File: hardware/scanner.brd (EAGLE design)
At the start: 65 x 56 mm, 9 parts, among them K1 PIN20X2, U1 EEPROM24, U2 TPS61165DBV

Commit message: update hat
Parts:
- removed CFG: (no value), FLYFISH:PIN_W_2
- added JP1, POWER: (no value), pinhead:1X02
- SWITCH: device FLYFISH:PIN_W_2 -> pinhead:1X02
- U1: value EEPROM24 -> CAT24C32WI-GT3; device FLYFISH:SOIC8 -> mbed-HDK-IC:SOIC127P600X175-8N
- moved SWITCH 51.6 mm to (28.0, 41.0), turned to 0 degrees
- moved U2 51.4 mm to (9.00, 44.0), turned to 180 degrees
- moved C1 8.25 mm to (56.0, 39.0), turned to 90 degrees
- moved R3 6.80 mm to (58.0, 39.0), turned to 90 degrees
- moved U1 6.76 mm to (59.0, 44.0), turned to 0 degrees
- moved R2 5.67 mm to (60.0, 39.0), turned to 270 degrees
- moved R1 3.16 mm to (62.0, 39.0), turned to 270 degrees
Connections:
- new net N$6: JP1.1, R3.2, U1.7
- net +3V3: now also R3.1; no longer R3.2
- net GND: now also JP1.2, POWER.1, SWITCH.1; no longer CFG.2, SWITCH.2
- net N$1: now also U1.5; no longer U1.6
- net N$2: now also POWER.2; no longer K1.27, R2.1, U1.5
- net N$3: now also K1.27, R2.1, U1.6; no longer CFG.1, R3.1, U1.7
- net N$4: now also SWITCH.2; no longer SWITCH.1
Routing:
- net +3V3: track 0.00 -> 57.2 mm
- net GND: track 0.00 -> 50.4 mm, vias 0 -> 2
- net N$1: track 0.00 -> 32.0 mm, vias 0 -> 1
- net N$3: track 0.00 -> 29.8 mm, vias 0 -> 1
- net N$5: track 0.00 -> 18.9 mm, vias 0 -> 1
- net N$6: track 0.00 -> 18.8 mm, vias 0 -> 1
- net +5V: track 0.00 -> 16.1 mm

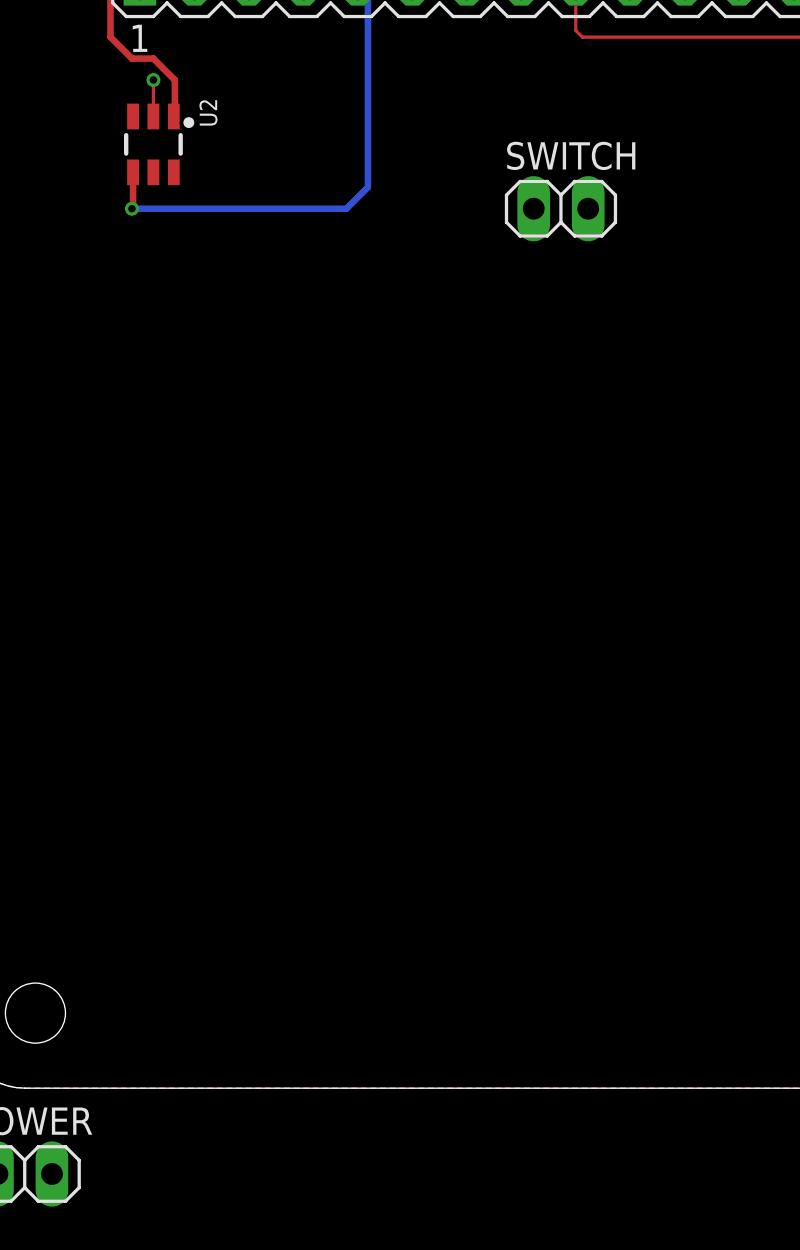
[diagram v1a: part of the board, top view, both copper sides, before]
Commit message: move eagle libs
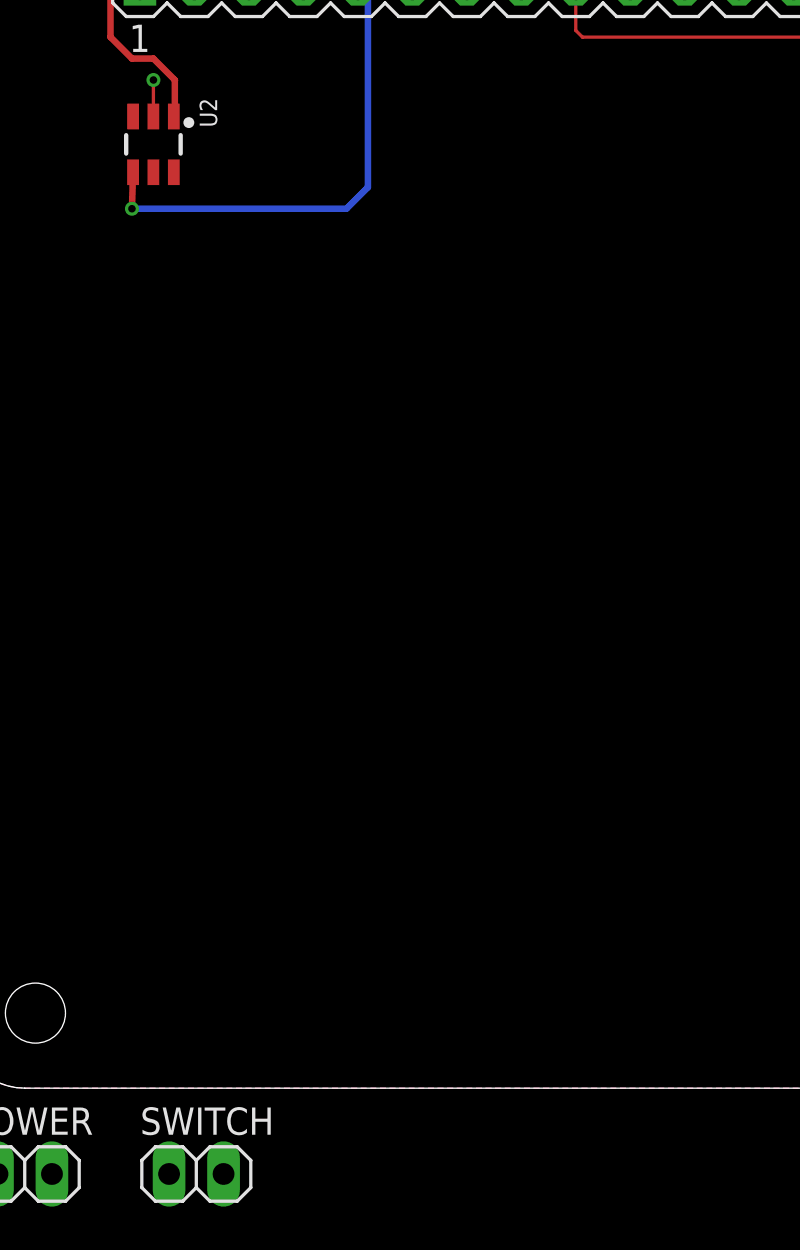
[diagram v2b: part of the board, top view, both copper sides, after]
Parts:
- moved SWITCH 48.1 mm to (11.0, -4.00)
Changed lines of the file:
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@@
 <drawing>
 <settings>
-<setting alwaysvectorfont="yes"/>
+<setting alwaysvectorfont="no"/>
 <setting keepoldvectorfont="yes"/>
 <setting verticaltext="up"/>
@@
 <attribute name="VALUE" x="60.286" y="37.984" size="1.27" layer="27" rot="R90"/>
 </element>
-<element name="SWITCH" library="pinhead" library_urn="urn:adsk.eagle:library:325" package="1X02" package3d_urn="urn:adsk.eagle:package:22435/2" value="" x="28" y="41" smashed="yes">
-<attribute name="NAME" x="25.3838" y="42.8288" size="1.27" layer="25" ratio="10"/>
-<attribute name="VALUE" x="25.46" y="37.825" size="1.27" layer="27"/>
+<element name="SWITCH" library="pinhead" library_urn="urn:adsk.eagle:library:325" package="1X02" package3d_urn="urn:adsk.eagle:package:22435/2" value="" x="11" y="-4" smashed="yes">
+<attribute name="NAME" x="8.3838" y="-2.1712" size="1.27" layer="25" ratio="10"/>
+<attribute name="VALUE" x="8.46" y="-7.175" size="1.27" layer="27"/>
 </element>
 <element name="JP1" library="pinhead" library_urn="urn:adsk.eagle:library:325" package="1X02" package3d_urn="urn:adsk.eagle:package:22435/2" value="" x="59" y="34" smashed="yes">
@@
 <wire x1="58" y1="36" x2="57" y2="37" width="0.1524" layer="16"/>
 <wire x1="57" y1="37" x2="57" y2="48" width="0.1524" layer="16"/>
-<via x="8" y="41" extent="1-16" drill="0.35"/>
-<wire x1="8.05" y1="41.05" x2="8" y2="41" width="0.1524" layer="1"/>
 <wire x1="19" y1="42" x2="18" y2="41" width="0.3048" layer="16"/>
-<wire x1="18" y1="41" x2="8" y2="41" width="0.3048" layer="16"/>
 <wire x1="18.53" y1="51.23" x2="19" y2="50.76" width="0.3048" layer="16"/>
 <wire x1="19" y1="50.76" x2="19" y2="42" width="0.3048" layer="16"/>
-<wire x1="8.05" y1="42.6999" x2="8.05" y2="41.05" width="0.3048" layer="1"/>
 <contactref element="POWER" pad="1"/>
+<wire x1="18" y1="41" x2="8" y2="41" width="0.3048" layer="16"/>
+<via x="8" y="41" extent="1-16" drill="0.35"/>
+<wire x1="8" y1="41" x2="8.05" y2="42.6999" width="0.3048" layer="1"/>
 <wire x1="43.93" y1="53.77" x2="49.01" y2="53.77" width="0" layer="19" extent="1-1"/>
 <wire x1="38.85" y1="51.23" x2="43.93" y2="53.77" width="0" layer="19" extent="1-1"/>
@@
 <wire x1="19" y1="50.76" x2="23.61" y2="53.77" width="0" layer="19" extent="16-16"/>
 <wire x1="13.45" y1="53.77" x2="18.53" y2="51.23" width="0" layer="19" extent="1-1"/>
-<wire x1="26.73" y1="41" x2="19" y2="42" width="0" layer="19" extent="16-16"/>
+<wire x1="9.73" y1="-4" x2="19" y2="42" width="0" layer="19" extent="16-16"/>
 <wire x1="1.73" y1="-4" x2="8" y2="41" width="0" layer="19" extent="16-16"/>
 </signal>
@@
 <contactref element="K1" pad="16"/>
 <contactref element="SWITCH" pad="2"/>
-<wire x1="29.27" y1="41" x2="26.15" y2="53.77" width="0" layer="19" extent="1-1"/>
+<wire x1="12.27" y1="-4" x2="26.15" y2="53.77" width="0" layer="19" extent="1-1"/>
 </signal>
 <signal name="N$5">

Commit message: update pcb
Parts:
- added C2: 220nF, resistor:C0805K
- added C3: 4.7μF, resistor:C0805K
- added C4: 1μF, resistor:C0805K
- added D1: 40V 550mA, adafruit:SOD-123
- added L1: 10 μH ±20% 1.49A, m-pad-2.1:D53LC
- added LED1, LED2: LW_W5SM-JYKY-JKQL-1, LW_W5SM-JYKY-JKQL-1:LWW5SMJYKYJKQL1
- added LED3, LED4, LED5: (no value), led:CHIP-LED0805
- added R4: 0.57, resistor:M0805
- added R5, R6, R7: 330, resistor:M0805
- moved POWER 30.6 mm to (33.0, -10.0)
- moved SWITCH 22.1 mm to (33.0, -6.00)
- moved C1 7.81 mm to (62.0, 34.0), turned to 270 degrees
- moved U2 5.83 mm to (6.00, 39.0)
- moved JP1 1.00 mm to (58.0, 34.0)
- moved R1 1.00 mm to (61.0, 39.0)
- moved R2 1.00 mm to (59.0, 39.0)
- moved R3 1.00 mm to (57.0, 39.0)
- moved U1 1.00 mm to (59.0, 45.0)
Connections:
- new net N$10: C4.1, D1.C, LED1.2
- new net N$11: LED1.1, LED2.2
- new net N$13: LED3.A, R5.2
- new net N$16: K1.13, R6.1
- new net N$17: LED4.A, R6.2
- new net N$18: LED5.A, R7.2
- new net N$19: K1.11, R5.1
- new net N$20: K1.15, R7.1
- new net N$7: C2.1, U2.5
- new net N$8: LED2.1, R4.1, U2.6
- new net N$9: D1.A, L1.2, U2.3
- net +5V: now also C3.1, L1.1
- net GND: now also C2.2, C3.2, C4.2, LED3.C, LED4.C, LED5.C, R4.2
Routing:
- net N$8: track 0.00 -> 79.7 mm
- net N$11: track 0.00 -> 55.4 mm
- net N$20: track 0.00 -> 52.1 mm, vias 0 -> 1
- net N$16: track 0.00 -> 50.6 mm, vias 0 -> 1
- net N$19: track 0.00 -> 50.2 mm, vias 0 -> 1
- net GND: track 50.4 -> 18.2 mm, vias 2 -> 6
- net N$10: track 0.00 -> 22.6 mm
- net N$9: track 0.00 -> 10.9 mm
- net N$5: track 18.9 -> 26.9 mm
- net +5V: track 16.1 -> 20.6 mm
- net +3V3: track 57.2 -> 61.5 mm
- net N$18: track 0.00 -> 2.00 mm
- net N$17: track 0.00 -> 2.00 mm
- net N$13: track 0.00 -> 2.00 mm
- net N$7: track 0.00 -> 1.70 mm
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- added copper zone on layer 2, net GND
- removed copper zone on layer 1, net GND
- removed copper zone on layer 16, net GND

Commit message: update pcb
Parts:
- removed POWER: (no value), pinhead:1X02
- added JP2: (no value), pinhead:2X02
- moved SWITCH 33.1 mm to (4.00, 10.0), turned to 180 degrees
- moved JP1 11.2 mm to (53.0, 44.0), turned to 90 degrees
- moved C1 3.61 mm to (59.0, 36.0), turned to 180 degrees
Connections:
- removed net N$2: POWER.2
- net +5V: now also JP2.1, JP2.2
- net GND: now also JP2.3, JP2.4; no longer POWER.1
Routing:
- net N$4: track 0.00 -> 63.6 mm
- net +5V: track 20.6 -> 61.9 mm
- net GND: track 18.2 -> 24.2 mm, vias 6 -> 8
- net N$6: track 17.2 -> 12.9 mm
- net +3V3: track 61.5 -> 63.1 mm
- net N$19: track 50.2 -> 51.4 mm
- net N$16: track 50.6 -> 51.8 mm
- net N$20: track 52.1 -> 53.3 mm

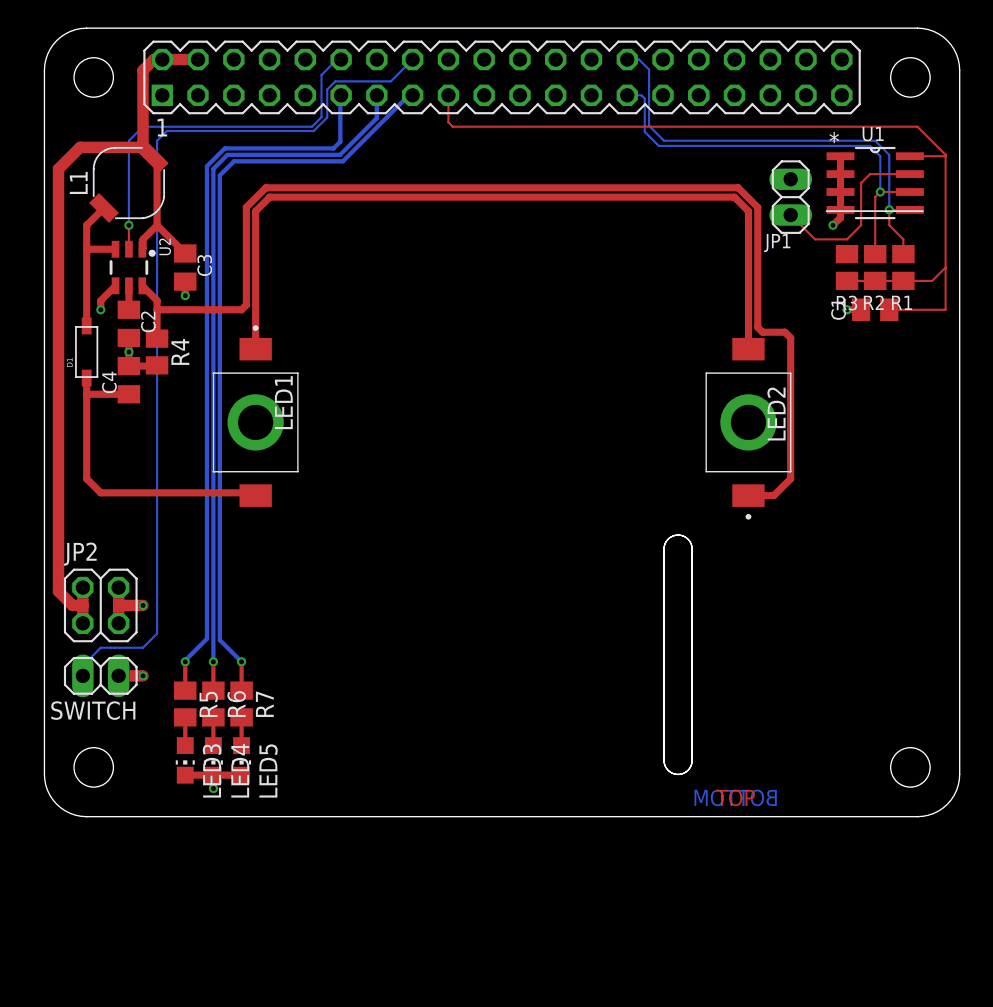
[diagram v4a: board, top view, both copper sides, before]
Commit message: added camera mounting holes
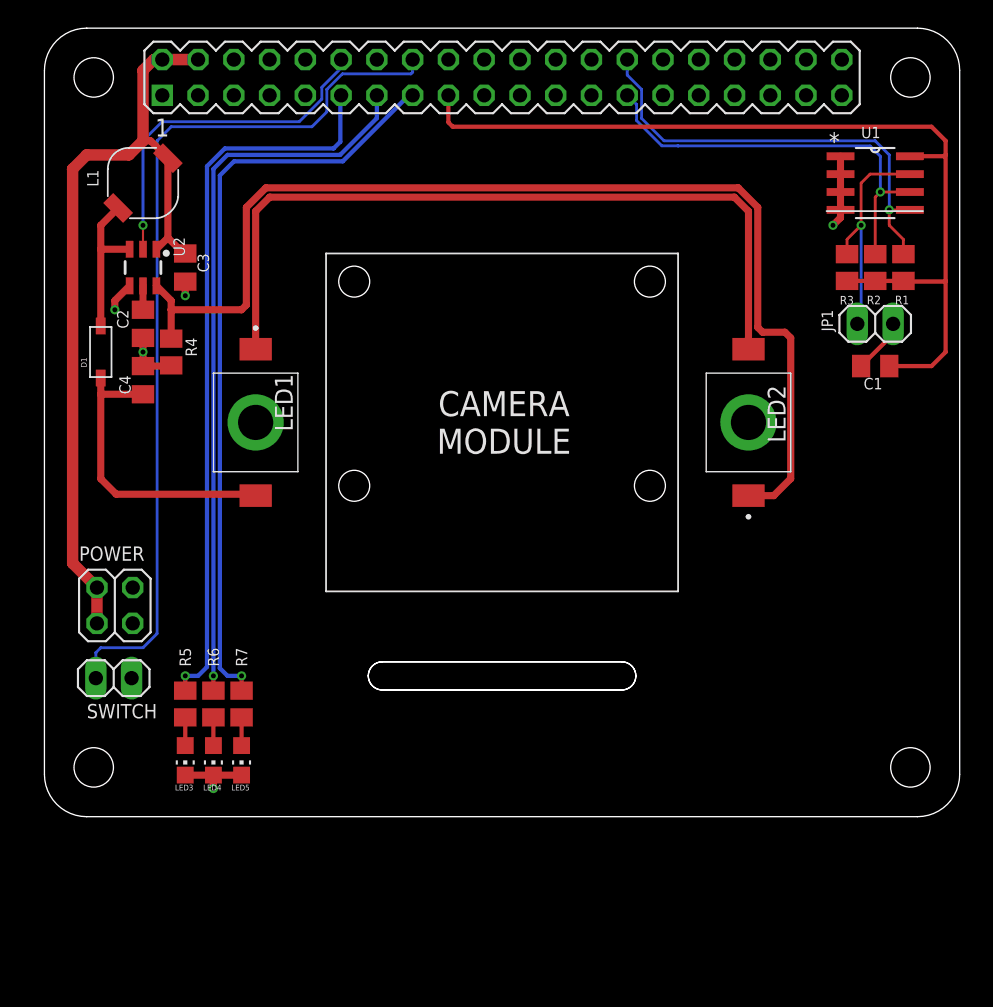
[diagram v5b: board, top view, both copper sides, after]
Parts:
- removed JP2: (no value), pinhead:2X02
- added POWER: (no value), pinhead:2X02
- moved JP1 10.8 mm to (59.0, 35.0), turned to 0 degrees
- moved C1 4.00 mm to (59.0, 32.0)
- moved C2 1.00 mm to (7.00, 35.0)
- moved C4 1.00 mm to (7.00, 31.0)
- moved D1 1.00 mm to (4.00, 33.0)
- moved L1 1.00 mm to (7.00, 45.0)
- moved R4 1.00 mm to (9.00, 33.0)
- moved U2 1.00 mm to (7.00, 39.0)
- moved SWITCH 0.93 mm to (4.92, 9.84)
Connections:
- net +5V: now also POWER.1, POWER.2; no longer JP2.1, JP2.2
- net GND: now also POWER.3, POWER.4; no longer JP2.3, JP2.4
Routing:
- net +3V3: track 63.1 -> 85.8 mm
- net N$6: track 12.9 -> 16.3 mm, vias 0 -> 1
- net +5V: track 61.9 -> 58.8 mm
- net GND: track 24.2 -> 21.2 mm, vias 8 -> 5
- net N$5: track 26.9 -> 25.0 mm
- net N$8: track 79.7 -> 78.8 mm
- net N$10: track 22.6 -> 21.8 mm
- net N$3: track 30.4 -> 29.6 mm
- net N$20: track 53.3 -> 53.9 mm
- net N$19: track 51.4 -> 51.9 mm
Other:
- outline, holes or cut-outs redrawn
- board text added: "CAMERA MODULE"
- board text removed: "BOTTOM"
- board text removed: "TOP"
